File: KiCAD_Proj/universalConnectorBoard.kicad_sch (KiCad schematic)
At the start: 3 parts, among them U1 SC0915_PicoDevModule, U2 TMC2209_MotorDriver, U3 TMC2209_MotorDriver

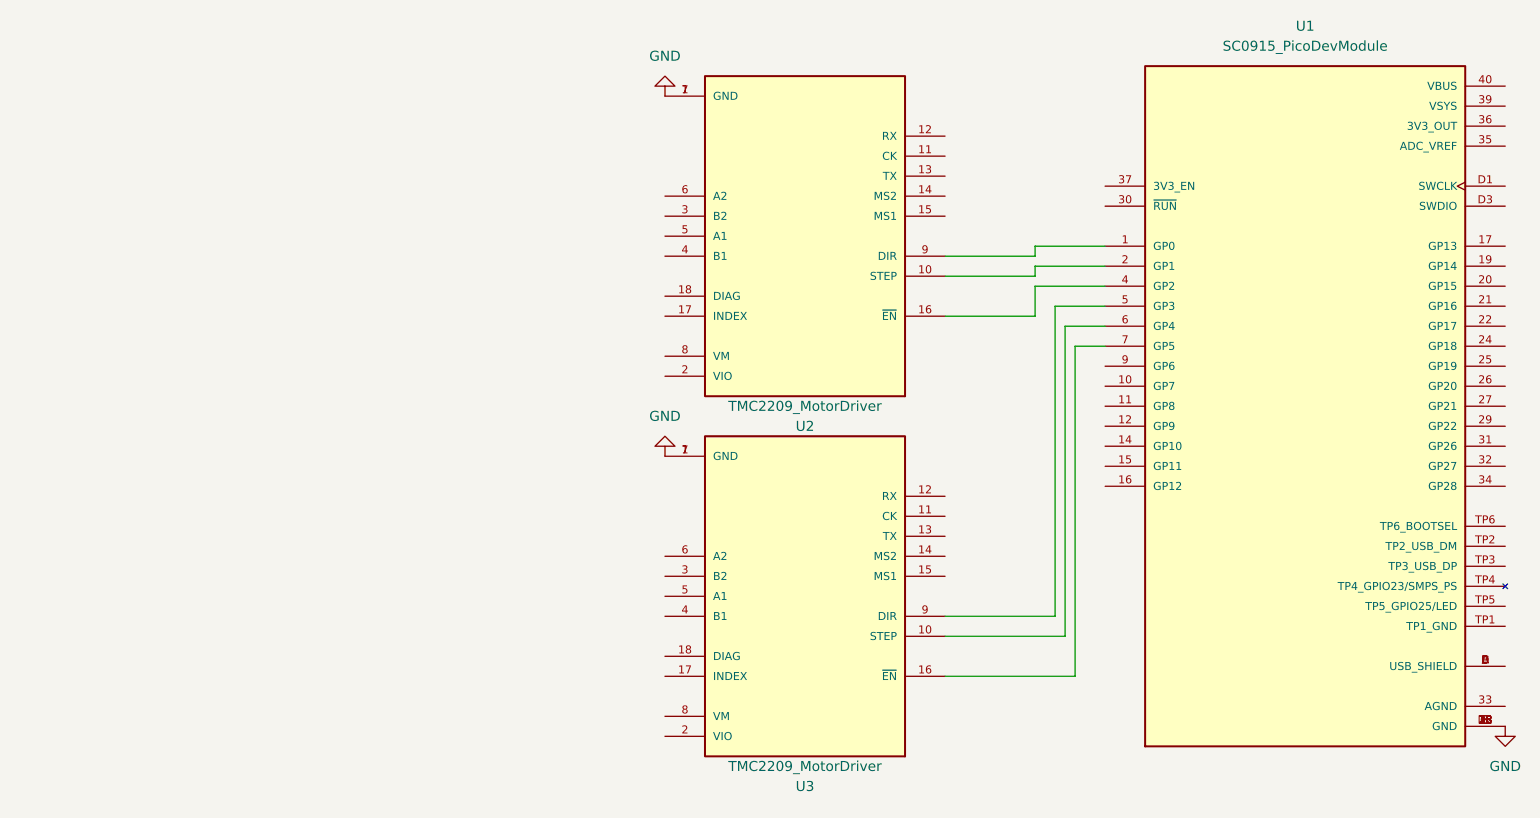
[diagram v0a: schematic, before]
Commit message: Add pico board footprint with through-hole and smd in one, just found it and thought it is something for the PCB.
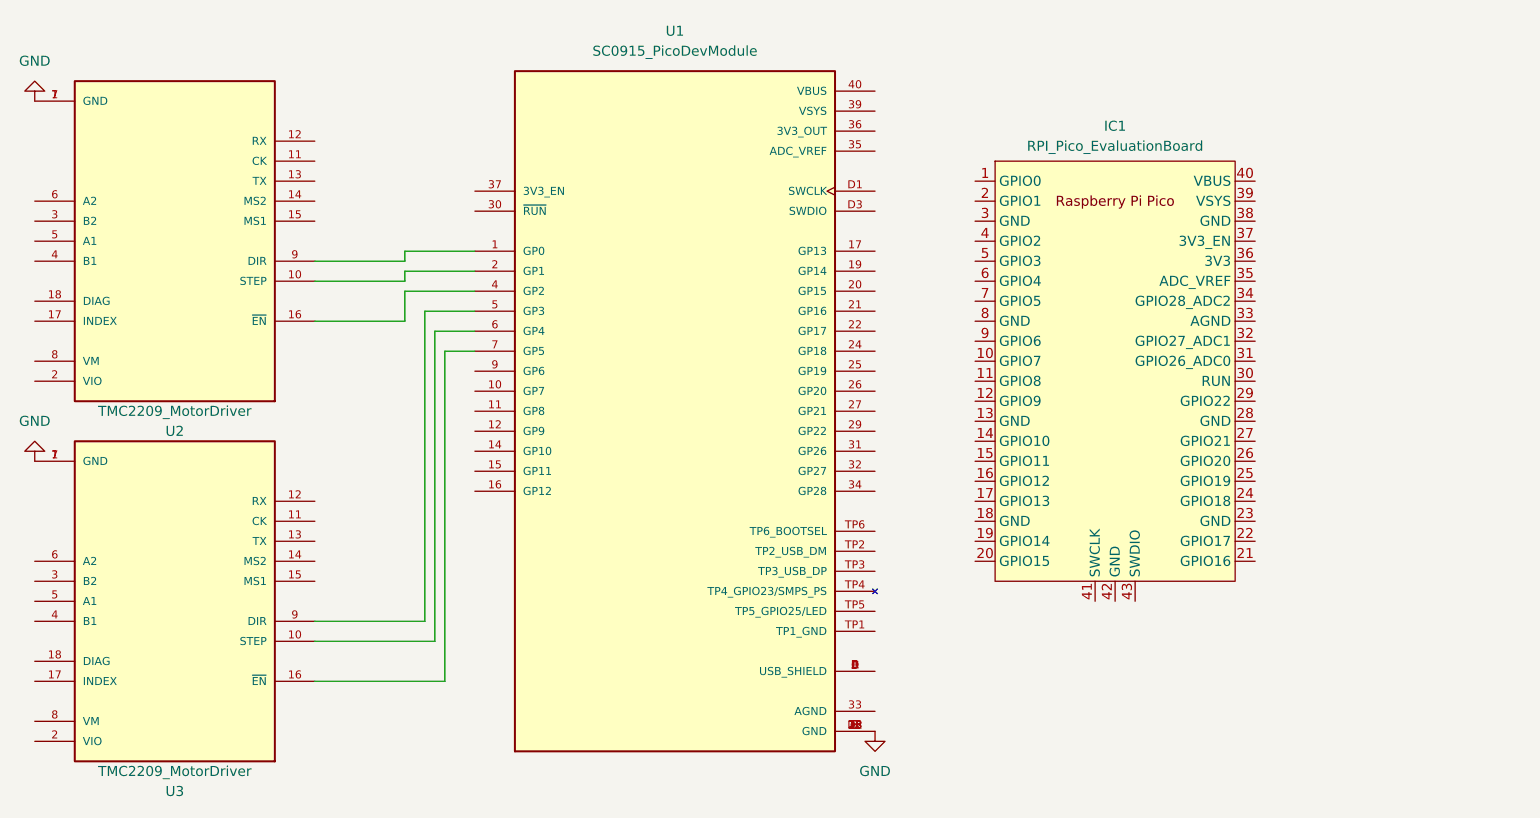
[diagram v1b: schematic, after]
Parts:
- added IC1: RPI_Pico_EvaluationBoard, Healthbot-Footprints:RPi_Pico_SMD_TH, symbol Healthbot-Symbols:RPI_Pico_EvaluationBoard
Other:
- moved on the sheet: U1, U2, U3

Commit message: Added several components and connections
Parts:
- removed U1: SC0915_PicoDevModule, SC0915:MODULE_SC0915, symbol SC0915:SC0915
- added C1: 0.10μF, symbol Device:C
- added IC2: SN74LV4052ADR, SOIC127P600X175-16N, symbol Healthbot-Symbols:SN74LV4052ADR
- added J1: 691401700003B, SamacSys_Parts:691401700003B, symbol Healthbot-Symbols:Terminal_Block3
- added J2: Display1, Connector_JST:JST_XH_S7B-XH-A_1x07_P2.50mm_Horizontal, symbol Connector:Conn_01x07_Pin
- added J3: Display2, Connector_JST:JST_XH_S7B-XH-A_1x07_P2.50mm_Horizontal, symbol Connector:Conn_01x07_Pin
- added J4, J5: Conn_01x02_Pin, symbol Connector:Conn_01x02_Pin
- added R1, R2, R3, R4, R5, R6, R7, R8: 100k, symbol Device:R
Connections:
- net GND: now also IC1.13 (GND), IC1.18 (GND), IC1.23 (GND), IC1.28 (GND), IC1.3 (GND), IC1.38 (GND), IC1.42 (GND), IC1.8 (GND), IC2.7 (GND_1), IC2.8 (GND_2), J2.7 (Pin_7), J3.7 (Pin_7)
- net MUX_TX1: now reaches U2.12 (RX)
- net MUX_TX1: now also IC2.12 (1Y0), R1.2
- net MUX_RX1: now reaches U2.13 (TX)
- net MUX_RX1: now also IC2.1 (2Y0), R5.2
- net MUX_TX2: now reaches U3.12 (RX)
- net MUX_TX2: now also IC2.14 (1Y1), R2.2
- net MUX_RX2: now reaches U3.13 (TX)
- net MUX_RX2: now also IC2.5 (2Y1), R6.2
- net TX_PICO: now reaches IC1.1 (GPIO0)
- net TX_PICO: now also IC2.13 (1-COM)
- net RX_PICO: now reaches IC1.2 (GPIO1)
- net RX_PICO: now also IC2.3 (2-COM)
- net A: now reaches IC1.4 (GPIO2)
- net A: now also IC2.10 (A)
- net B: now reaches IC1.5 (GPIO3)
- net B: now also IC2.9 (B)
- net INH: now reaches IC1.6 (GPIO4)
- net INH: now also IC2.6 (INH)
- new net: C1.2, IC2.16 (VCC)
- new net +3V3: J2.6 (Pin_6), J3.6 (Pin_6)
- new net DIsplay_DC: J3.2 (Pin_2)
- new net Display1_CS: J2.1 (Pin_1)
- new net Display1_RES: J2.3 (Pin_3)
- new net Display2_CS: J3.1 (Pin_1)
- new net Display2_RES: J3.3 (Pin_3)
- new net Display_DC: J2.2 (Pin_2)
- new net Display_SCL: J2.5 (Pin_5), J3.5 (Pin_5)
- new net Display_SDA: J2.4 (Pin_4), J3.4 (Pin_4)
- new net MUX_RX3: IC2.2 (2Y2), J4.2 (Pin_2), R7.2
- new net MUX_RX4: IC2.4 (2Y3), J5.2 (Pin_2), R8.2
- new net MUX_TX3: IC2.15 (1Y2), J4.1 (Pin_1), R3.2
- new net MUX_TX4: IC2.11 (1Y3), J5.1 (Pin_1), R4.2
- new net VCC: C1.1, R1.1, R2.1, R3.1, R4.1, R5.1, R6.1, R7.1, R8.1
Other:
- moved on the sheet: IC1, U2, U3

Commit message: Added more components
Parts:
- added J6: Conn_01x04_Pin, symbol Connector:Conn_01x04_Pin
- added U1: L7805, symbol Regulator_Linear:L7805
- added U2: LM1117DT-3.3, Package_TO_SOT_SMD:TO-252-3_TabPin2, symbol Regulator_Linear:LM1117DT-3.3
- R1, R2, R3, R4, R5, R6, R7, R8: footprint (none) -> Resistor_SMD:R_0603_1608Metric_Pad0.98x0.95mm_HandSolder
- renumbered U2 to U3, U3 to U4
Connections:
- net GND: now also J1.3, J1.4
- net +12V: now reaches J1.1
- net +12V: now also J1.2
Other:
- moved on the sheet: J1

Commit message: Multiple additions
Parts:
- removed J4, J5: Conn_01x02_Pin, symbol Connector:Conn_01x02_Pin
- added C2, C3: C, Capacitor_SMD:C_0603_1608Metric_Pad1.08x0.95mm_HandSolder, symbol Device:C
- added J4: GPIO, Connector_PinHeader_2.54mm:PinHeader_2x20_P2.54mm_Vertical_SMD, symbol Connector_Generic:Conn_02x20_Odd_Even
- added J5: Ledstrip2, Connector_JST:JST_XH_S3B-XH-A_1x03_P2.50mm_Horizontal, symbol Connector:Conn_01x03_Pin
- added J7: MUX4_UART, Connector_PinSocket_2.54mm:PinSocket_1x04_P2.54mm_Vertical, symbol Connector:Conn_01x04_Pin
- added J8: Ledstrip1, Connector_JST:JST_XH_S4B-XH-A_1x04_P2.50mm_Horizontal, symbol Connector:Conn_01x04_Pin
- added R10, R9: 470, Resistor_SMD:R_0603_1608Metric_Pad0.98x0.95mm_HandSolder, symbol Device:R
- C1: footprint (none) -> Capacitor_SMD:C_0603_1608Metric_Pad1.08x0.95mm_HandSolder
- J6: value Conn_01x04_Pin -> MUX3_UART; footprint (none) -> Connector_PinSocket_2.54mm:PinSocket_1x04_P2.54mm_Vertical
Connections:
- net DIsplay_DC is gone; now on net Display_DC: J3.2 (Pin_2)
- net Display1_RES is gone; now on net Display_SDA: J2.3 (Pin_3)
- net Display2_RES is gone; now on net Display_SDA: J3.3 (Pin_3)
- net +12V: now also C2.2, J8.4 (Pin_4)
- net Display1_CS: now also IC1.12 (GPIO9)
- net Display2_CS: now also IC1.17 (GPIO13)
- net Display_DC: now also IC1.11 (GPIO8)
- net Display_SCL: now also IC1.15 (GPIO11), J2.4 (Pin_4), J3.4 (Pin_4); no longer J2.5 (Pin_5), J3.5 (Pin_5)
- net Display_SDA: now also IC1.14 (GPIO10); no longer J2.4 (Pin_4), J3.4 (Pin_4)
- net GND: now also J6.4 (Pin_4), C2.1, C3.1, J4.14 (Pin_14), J4.20 (Pin_20), J4.25 (Pin_25), J4.30 (Pin_30), J4.34 (Pin_34), J4.39 (Pin_39), J4.6 (Pin_6), J4.9 (Pin_9), J5.1 (Pin_1), J7.4 (Pin_4), J8.1 (Pin_1), J8.2 (Pin_2)
- net MUX_RX3: now also J6.3 (Pin_3)
- net MUX_RX4: now also J7.3 (Pin_3)
- net MUX_TX3: now also J6.2 (Pin_2)
- net MUX_TX4: now also J7.2 (Pin_2)
- net VCC: now also J6.1 (Pin_1), J7.1 (Pin_1)
- net Display_RES: now reaches IC1.16 (GPIO12)
- net Display_RES: now also J2.5 (Pin_5), J3.5 (Pin_5)
- net Ledstrip1_DATA: now reaches IC1.7 (GPIO5)
- net Ledstrip1_DATA: now also R9.2
- net Ledstrip2_DATA: now reaches IC1.9 (GPIO6)
- net Ledstrip2_DATA: now also R10.2
- new net: J5.2 (Pin_2), R10.1
- new net: J8.3 (Pin_3), R9.1
- new net +3.3V: J4.1 (Pin_1), J4.17 (Pin_17)
- new net +5V: C3.2, J4.2 (Pin_2), J4.4 (Pin_4), J5.3 (Pin_3)
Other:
- note added: "BO/BI"
- moved on the sheet: J6

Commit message: Added lots of connections
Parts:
- removed U1: L7805, symbol Regulator_Linear:L7805
- removed U2: LM1117DT-3.3, Package_TO_SOT_SMD:TO-252-3_TabPin2, symbol Regulator_Linear:LM1117DT-3.3
- added JP2: Jumper_3_Bridged12, Connector_PinHeader_2.54mm:PinHeader_1x03_P2.54mm_Vertical, symbol Jumper:Jumper_3_Bridged12
- C2, C3: value C -> 1000μF
- J4: value GPIO -> RPI4
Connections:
- net +3.3V: now also JP2.1 (A)
- net +5V: now also JP2.3 (B)
- net GND: now also C1.2
- net RX_PICO: now also IC1.22 (GPIO17); no longer IC1.2 (GPIO1)
- net TX_PICO: now also IC1.21 (GPIO16); no longer IC1.1 (GPIO0)
- net VCC: no longer C1.1
- net RXD_PI4: now reaches J4.10 (Pin_10)
- net RXD_PI4: now also IC1.1 (GPIO0)
- net TXD_PI4: now reaches J4.8 (Pin_8)
- net TXD_PI4: now also IC1.2 (GPIO1)
- net at IC2.16 (VCC): now also C1.1, JP2.2 (C); no longer C1.2
- net MD1_STEP: now reaches U3.10 (STEP)
- net MD1_EN: now reaches U3.16 (~{EN})
- net MD1_DIR: now reaches U3.9 (DIR)
- net MD2_STEP: now reaches U4.10 (STEP)
- net MD2_EN: now reaches U4.16 (~{EN})
- net MD3_STEP: now reaches U4.9 (DIR)
- net Leds_Cheeks: now reaches IC1.10 (GPIO7)
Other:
- note added: "Leds_Cheeks?"
- note added: "UART0 dubbel!!!!"
- moved on the sheet: C1, C2, C3, IC1, IC2, J2, J3, J4, J5, J8, R10, R9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

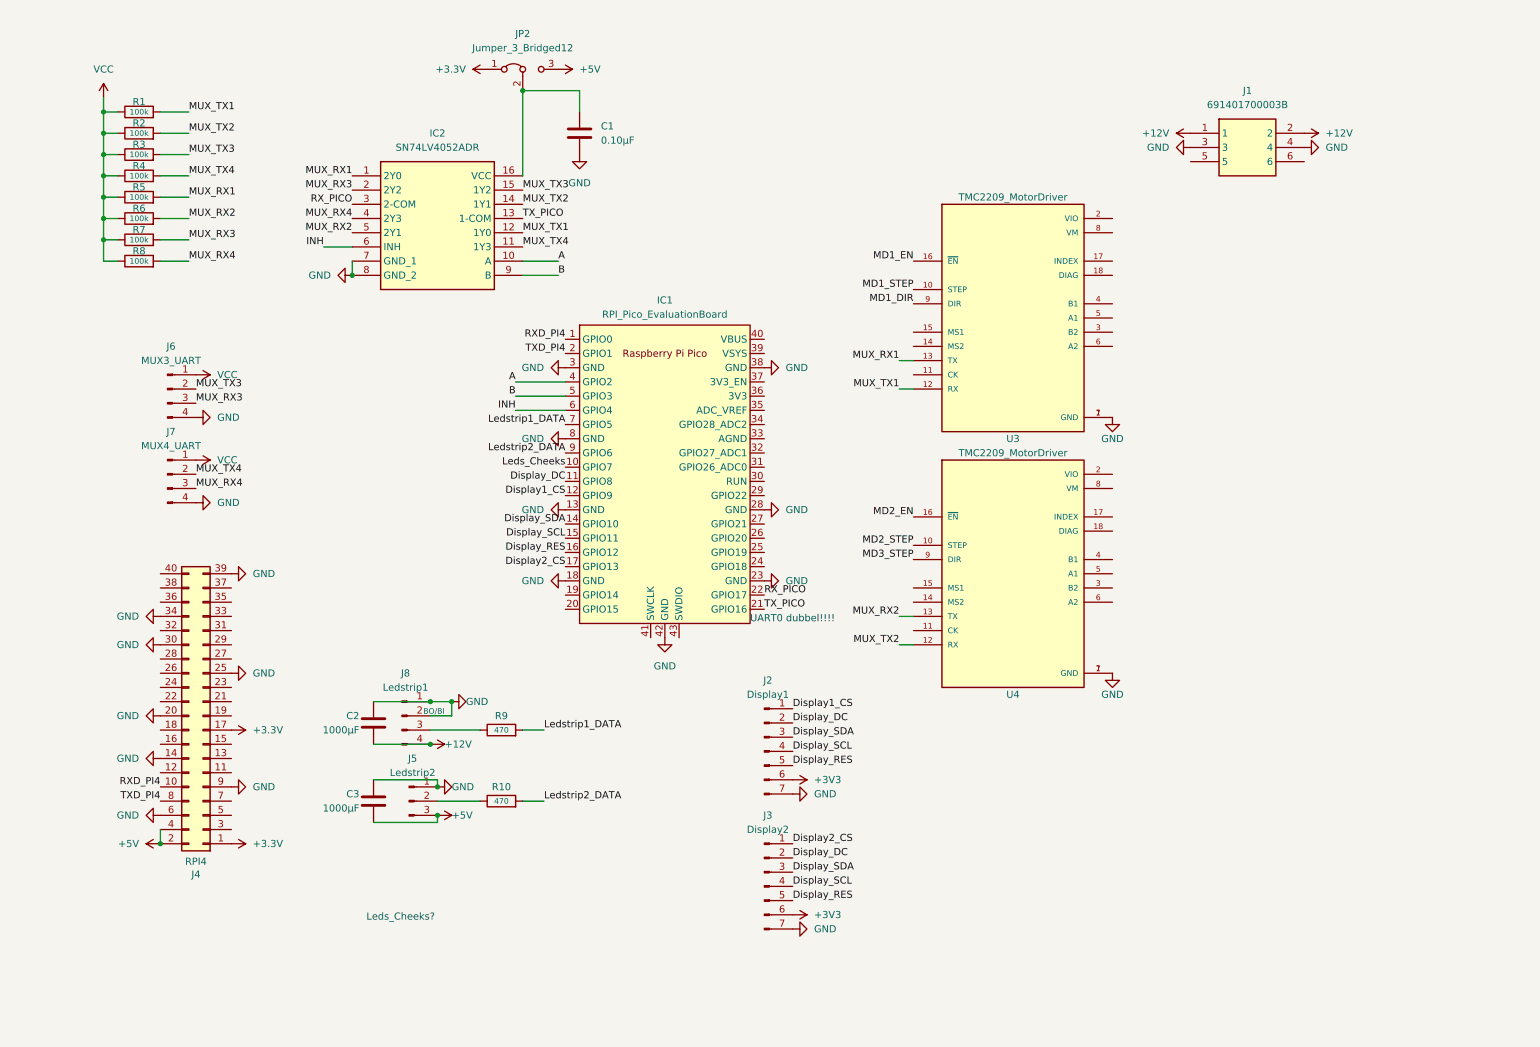
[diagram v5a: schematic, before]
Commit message: All pico GPIO pins assigned
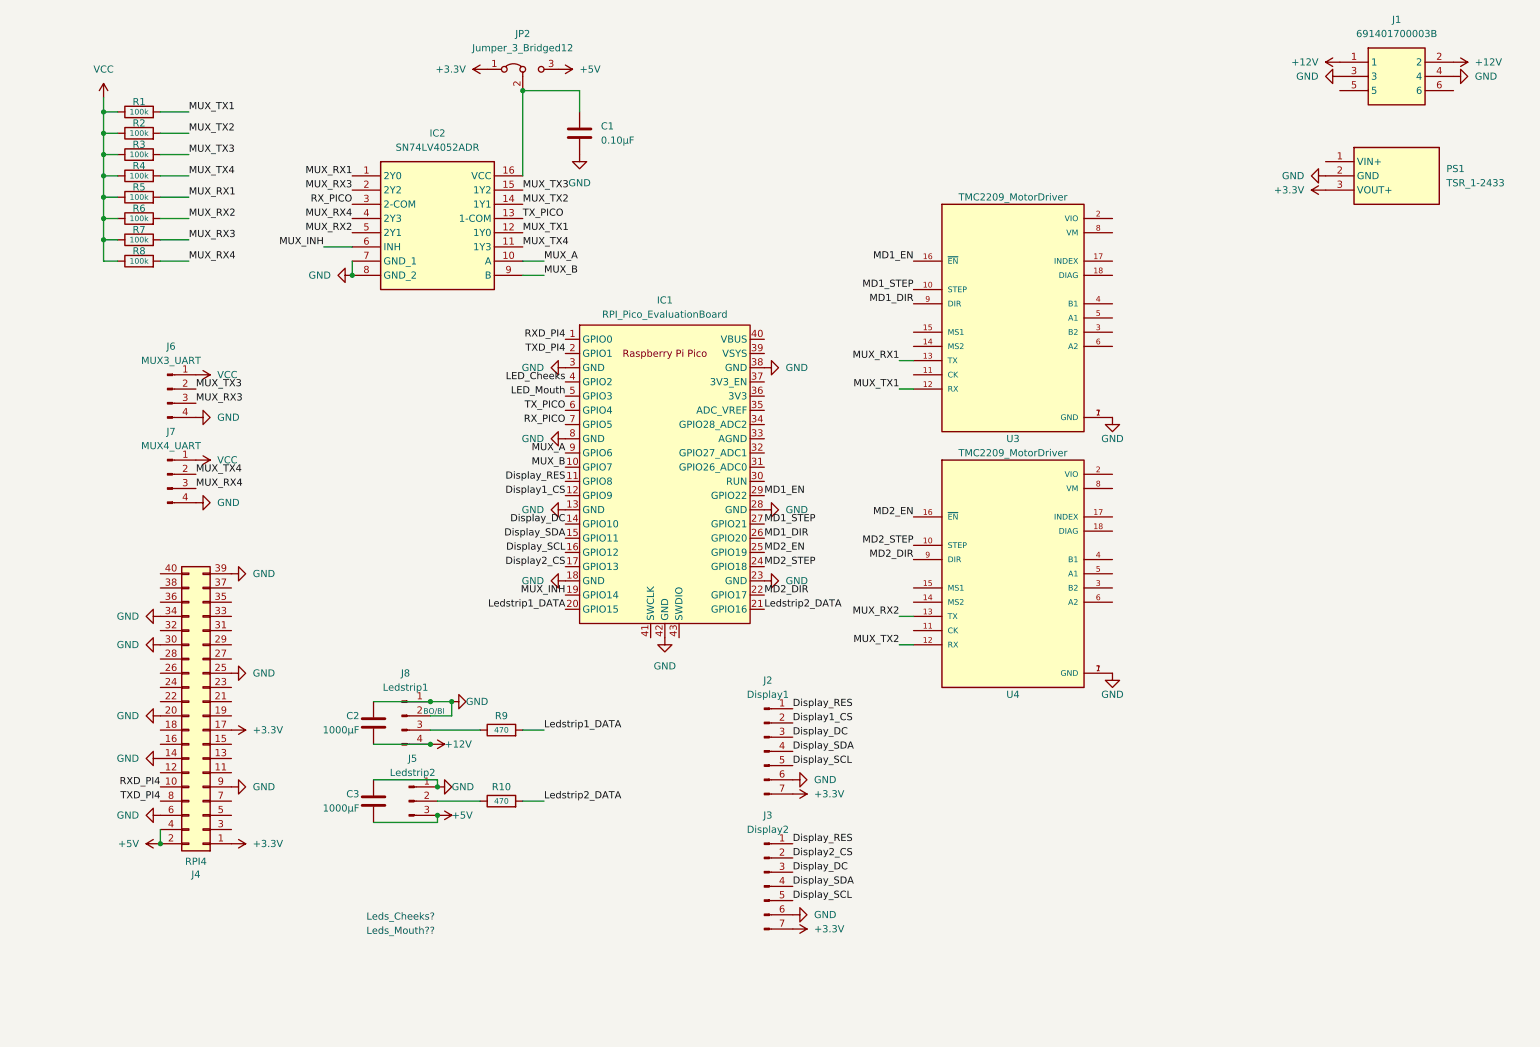
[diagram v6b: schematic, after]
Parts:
- added PS1: TSR_1-2433, TSR-1-2433, symbol Healthbot-Symbols:DC-DC_3.3V
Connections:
- net +3V3 is gone; now on net GND: J2.6 (Pin_6), J3.6 (Pin_6)
- net +3.3V: now also J2.7 (Pin_7), J3.7 (Pin_7), PS1.3 (VOUT+)
- net Display1_CS: now also J2.2 (Pin_2); no longer J2.1 (Pin_1)
- net Display2_CS: now also J3.2 (Pin_2); no longer J3.1 (Pin_1)
- net Display_DC: now also IC1.14 (GPIO10), J2.3 (Pin_3), J3.3 (Pin_3); no longer IC1.11 (GPIO8), J2.2 (Pin_2), J3.2 (Pin_2)
- net Display_RES: now also IC1.11 (GPIO8), J2.1 (Pin_1), J3.1 (Pin_1); no longer IC1.16 (GPIO12), J2.5 (Pin_5), J3.5 (Pin_5)
- net Display_SCL: now also IC1.16 (GPIO12), J2.5 (Pin_5), J3.5 (Pin_5); no longer IC1.15 (GPIO11), J2.4 (Pin_4), J3.4 (Pin_4)
- net Display_SDA: now also IC1.15 (GPIO11), J2.4 (Pin_4), J3.4 (Pin_4); no longer IC1.14 (GPIO10), J2.3 (Pin_3), J3.3 (Pin_3)
- net GND: now also PS1.2 (GND); no longer J2.7 (Pin_7), J3.7 (Pin_7)
- net Ledstrip1_DATA: now also IC1.20 (GPIO15); no longer IC1.7 (GPIO5)
- net Ledstrip2_DATA: now also IC1.21 (GPIO16); no longer IC1.9 (GPIO6)
- net MD1_DIR: now also IC1.26 (GPIO20)
- net MD1_EN: now also IC1.29 (GPIO22)
- net MD1_STEP: now also IC1.27 (GPIO21)
- net MD2_EN: now also IC1.25 (GPIO19)
- net MD2_STEP: now also IC1.24 (GPIO18)
- net RX_PICO: now also IC1.7 (GPIO5); no longer IC1.22 (GPIO17)
- net TX_PICO: now also IC1.6 (GPIO4); no longer IC1.21 (GPIO16)
- net MUX_INH: now reaches IC1.19 (GPIO14)
- net MUX_INH: now also IC2.6 (INH)
- net A renamed LED_Cheeks
- net LED_Cheeks: no longer IC2.10 (A)
- net B renamed LED_Mouth
- net LED_Mouth: no longer IC2.9 (B)
- removed net INH: IC1.6 (GPIO4), IC2.6 (INH)
- net Leds_Cheeks renamed MUX_B
- net MUX_B: now also IC2.9 (B)
- net MD3_STEP renamed MD2_DIR
- net MD2_DIR: now also IC1.22 (GPIO17)
- new net MUX_A: IC1.9 (GPIO6), IC2.10 (A)
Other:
- note added: "Leds_Mouth??"
- note removed: "UART0 dubbel!!!!"
- moved on the sheet: J1
